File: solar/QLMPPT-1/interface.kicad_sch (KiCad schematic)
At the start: 0 parts

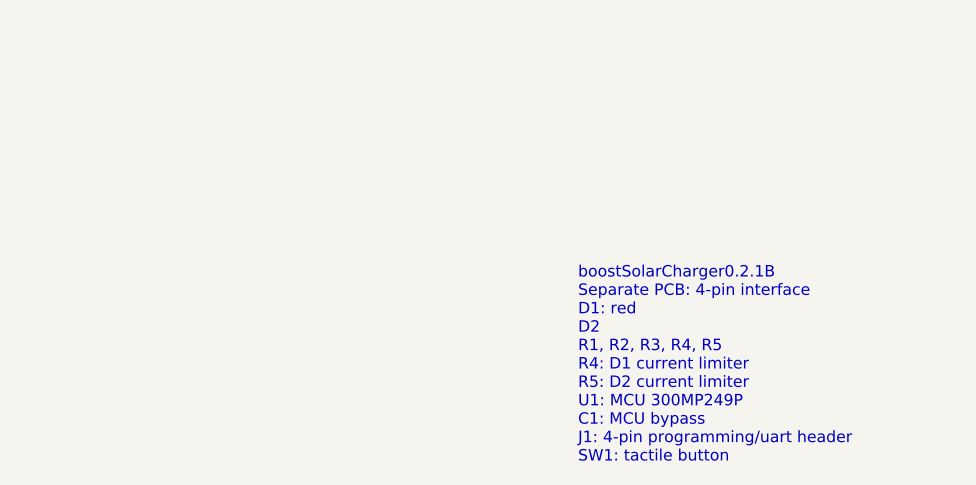
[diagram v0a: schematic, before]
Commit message: Sketching boost converter
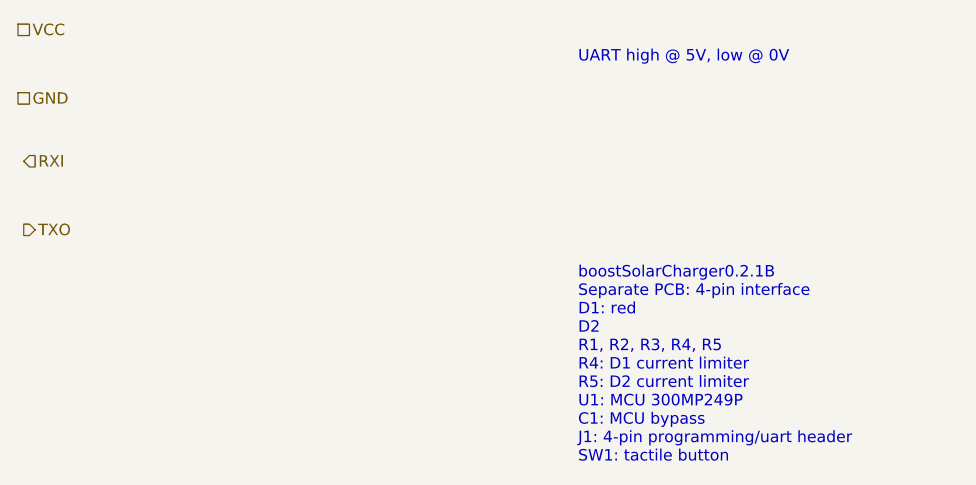
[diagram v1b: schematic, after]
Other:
- note added: "UART high @ 5V, low @ 0V"
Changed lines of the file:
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@@
 (kicad_sch (version 20211123) (generator eeschema)
   (paper "A4")
+  (text "UART high @ 5V, low @ 0V" (at 130.81 55.88 0)
+    (effects (font (size 1.27 1.27)) (justify left bottom))
+  )
   (text "boostSolarCharger0.2.1B\nSeparate PCB: 4-pin interface\nD1: red\nD2\nR1, R2, R3, R4, R5\nR4: D1 current limiter\nR5: D2 current limiter\nU1: MCU 300MP249P\nC1: MCU bypass\nJ1: 4-pin programming/uart header\nSW1: tactile button\n"
     (at 130.81 100.33 0)
     (effects (font (size 1.27 1.27)) (justify left bottom))
   )
+  (hierarchical_label "RXI" (shape input) (at 69.215 66.675 0)
+    (effects (font (size 1.27 1.27)) (justify left))
+  )
+  (hierarchical_label "VCC" (shape passive) (at 68.58 52.07 0)
+    (effects (font (size 1.27 1.27)) (justify left))
+  )
+  (hierarchical_label "GND" (shape passive) (at 68.58 59.69 0)
+    (effects (font (size 1.27 1.27)) (justify left))
+  )
+  (hierarchical_label "TXO" (shape output) (at 69.215 74.295 0)
+    (effects (font (size 1.27 1.27)) (justify left))
+  )
   (sheet_instances
